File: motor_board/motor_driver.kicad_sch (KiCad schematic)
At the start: 15 parts, among them U1 DRV8833PW, U2 DCP3603BCMR

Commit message: Began motor board layour
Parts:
- added C7: 2.2u, Capacitor_SMD:C_0805_2012Metric_Pad1.18x1.45mm_HandSolder, symbol Device:C
- C4: value 22u -> 4.7u
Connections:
- net GND: now also C7.2
- net VCC: now also C7.1
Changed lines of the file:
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@@
+	)
+	(junction
+		(at 168.91 46.99)
+		(diameter 0)
+		(color 0 0 0 0)
+	)
+	(junction
+		(at 168.91 36.83)
+		(diameter 0)
+		(color 0 0 0 0)
 	)
 	(junction
@@
 	(wire
 		(pts
-			(xy 121.92 29.21) (xy 124.46 29.21)
+			(xy 168.91 45.72) (xy 168.91 46.99)
 		)
 		(stroke
@@
 	(wire
 		(pts
-			(xy 160.02 35.56) (xy 160.02 36.83)
+			(xy 121.92 29.21) (xy 124.46 29.21)
 		)
 		(stroke
@@
 	(wire
 		(pts
-			(xy 85.09 38.1) (xy 85.09 39.37)
+			(xy 160.02 35.56) (xy 160.02 36.83)
 		)
 		(stroke
@@
 	(wire
 		(pts
-			(xy 95.25 33.02) (xy 95.25 31.75)
+			(xy 85.09 38.1) (xy 85.09 39.37)
 		)
 		(stroke
@@
 	(wire
 		(pts
-			(xy 134.62 46.99) (xy 146.05 46.99)
+			(xy 95.25 33.02) (xy 95.25 31.75)
 		)
 		(stroke
@@
 	(wire
 		(pts
-			(xy 146.05 36.83) (xy 146.05 46.99)
+			(xy 134.62 46.99) (xy 146.05 46.99)
 		)
 		(stroke
@@
 	(wire
 		(pts
-			(xy 83.82 31.75) (xy 83.82 30.48)
+			(xy 146.05 36.83) (xy 146.05 46.99)
 		)
 		(stroke
@@
 	(wire
 		(pts
-			(xy 85.09 46.99) (xy 96.52 46.99)
+			(xy 83.82 31.75) (xy 83.82 30.48)
 		)
 		(stroke
@@
 	(wire
 		(pts
-			(xy 134.62 36.83) (xy 134.62 39.37)
+			(xy 85.09 46.99) (xy 96.52 46.99)
 		)
 		(stroke
@@
 	(wire
 		(pts
-			(xy 134.62 29.21) (xy 146.05 29.21)
+			(xy 134.62 36.83) (xy 134.62 39.37)
 		)
 		(stroke
@@
 	(wire
 		(pts
-			(xy 132.08 29.21) (xy 134.62 29.21)
+			(xy 134.62 29.21) (xy 146.05 29.21)
 		)
 		(stroke
@@
 	(wire
 		(pts
-			(xy 95.25 22.86) (xy 95.25 24.13)
+			(xy 132.08 29.21) (xy 134.62 29.21)
 		)
 		(stroke
@@
 	(wire
 		(pts
+			(xy 95.25 22.86) (xy 95.25 24.13)
+		)
+		(stroke
+			(width 0)
+			(type default)
+		)
+	)
+	(wire
+		(pts
 			(xy 146.05 29.21) (xy 149.86 29.21)
+		)
+		(stroke
+			(width 0)
+			(type default)
+		)
+	)
+	(wire
+		(pts
+			(xy 168.91 36.83) (xy 168.91 38.1)
 		)
 		(stroke
@@
 			)
 		)
-		(property "Value" "22u"
+		(property "Value" "4.7u"
 			(at 149.86 34.2899 0)
 			(effects
@@
 					(unit 1)
 				)
+			)
+		)
+	)
+	(symbol
+		(lib_id "Device:C")
+		(at 168.91 41.91 0)
+		(unit 1)
+		(exclude_from_sim no)
+		(in_bom yes)
+		(on_board yes)
+		(dnp no)
+		(property "Reference" "C7"
+			(at 162.814 40.64 0)
+			(effects
+				(font
+					(size 1.27 1.27)
+				)
+				(justify left)
+			)
+		)
+		(property "Value" "2.2u"
+			(at 162.052 42.672 0)
+			(effects
+				(font
+					(size 1.27 1.27)
+				)
+				(justify left)
+			)
+		)
+		(property "Footprint" "Capacitor_SMD:C_0805_2012Metric_Pad1.18x1.45mm_HandSolder"
+			(at 169.8752 45.72 0)
+			(effects
+				(font
+					(size 1.27 1.27)
+				)
+				(hide yes)
+			)
+		)
+		(property "Datasheet" "~"
+			(at 168.91 41.91 0)
+			(effects
+				(font
+					(size 1.27 1.27)
+				)
+				(hide yes)
+			)
+		)
+		(property "Description" "Unpolarized capacitor"
+			(at 168.91 41.91 0)
+			(effects
+				(font
+					(size 1.27 1.27)
+				)
+				(hide yes)
+			)
+		)
+		(pin "2"
+		)
+		(pin "1"
+		)
+		(instances
+			(project "motor_board"
+				(path "/b6fc042c-8182-4315-99f5-f408711f7d41/3ee30c65-97d4-477c-ab34-3fea9180008b"
+					(reference "C7")
+					(unit 1)
+				)

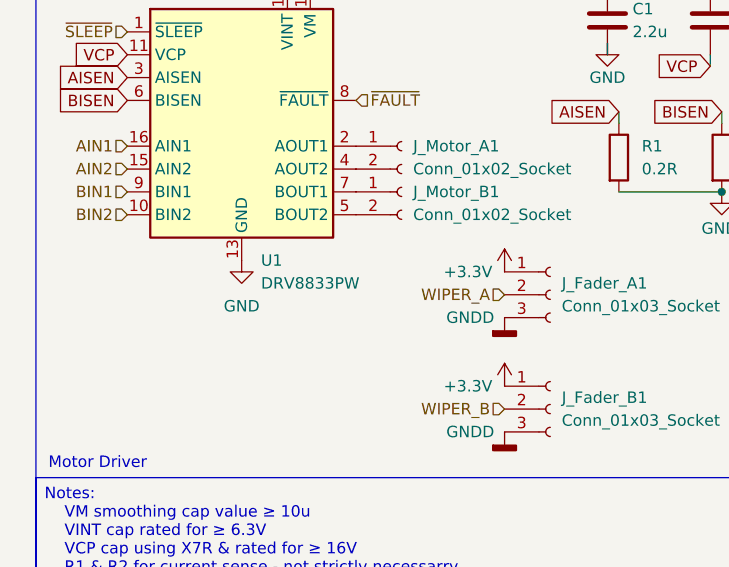
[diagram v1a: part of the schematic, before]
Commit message: Finished motor board PCB
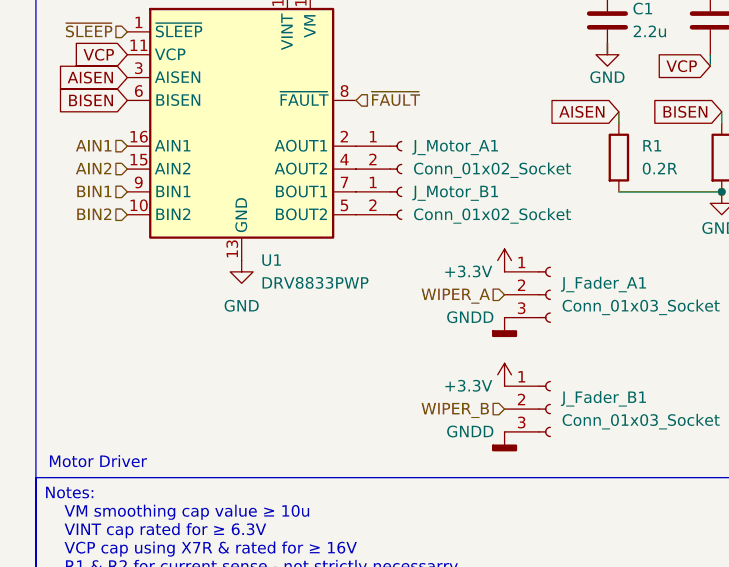
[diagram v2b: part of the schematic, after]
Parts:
- removed U1: DRV8833PW, Package_SO:TSSOP-16-1EP_4.4x5mm_P0.65mm_EP3x3mm_ThermalVias, symbol Driver_Motor:DRV8833PW
- added U1: DRV8833PWP, Package_SO:HTSSOP-16-1EP_4.4x5mm_P0.65mm_EP3.4x5mm_Mask2.46x2.31mm_ThermalVias, symbol Driver_Motor:DRV8833PWP
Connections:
- net AIN1: now also U1.16 (AIN1)
- net AIN2: now also U1.15 (AIN2)
- net AISEN: now also U1.3 (AISEN)
- net BIN1: now also U1.9 (BIN1)
- net BIN2: now also U1.10 (BIN2)
- net BISEN: now also U1.6 (BISEN)
- net GND: now also U1.13 (GND), U1.17 (GND)
- net VCP: now also U1.11 (VCP)
- net VDC: now also U1.12 (VM)
- net VINT: now also U1.14 (VINT)
- net ~{FAULT}: now also U1.8 (~{FAULT})
- net ~{SLEEP}: now also U1.1 (~{SLEEP})
- net at J_Motor_A1.1 (Pin_1): now also U1.2 (AOUT1)
- net at J_Motor_A1.2 (Pin_2): now also U1.4 (AOUT2)
- net at J_Motor_B1.2 (Pin_2): now also U1.5 (BOUT2)
- net at J_Motor_B1.1 (Pin_1): now also U1.7 (BOUT1)

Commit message: Modified motor_board; larger DC/DC inductor
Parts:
- L1: footprint Inductor_SMD:L_Wuerth_MAPI-5030 -> 744393665033:744393665033
